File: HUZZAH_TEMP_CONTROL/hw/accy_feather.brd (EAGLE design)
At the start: 50.8 x 22.9 mm, 26 parts

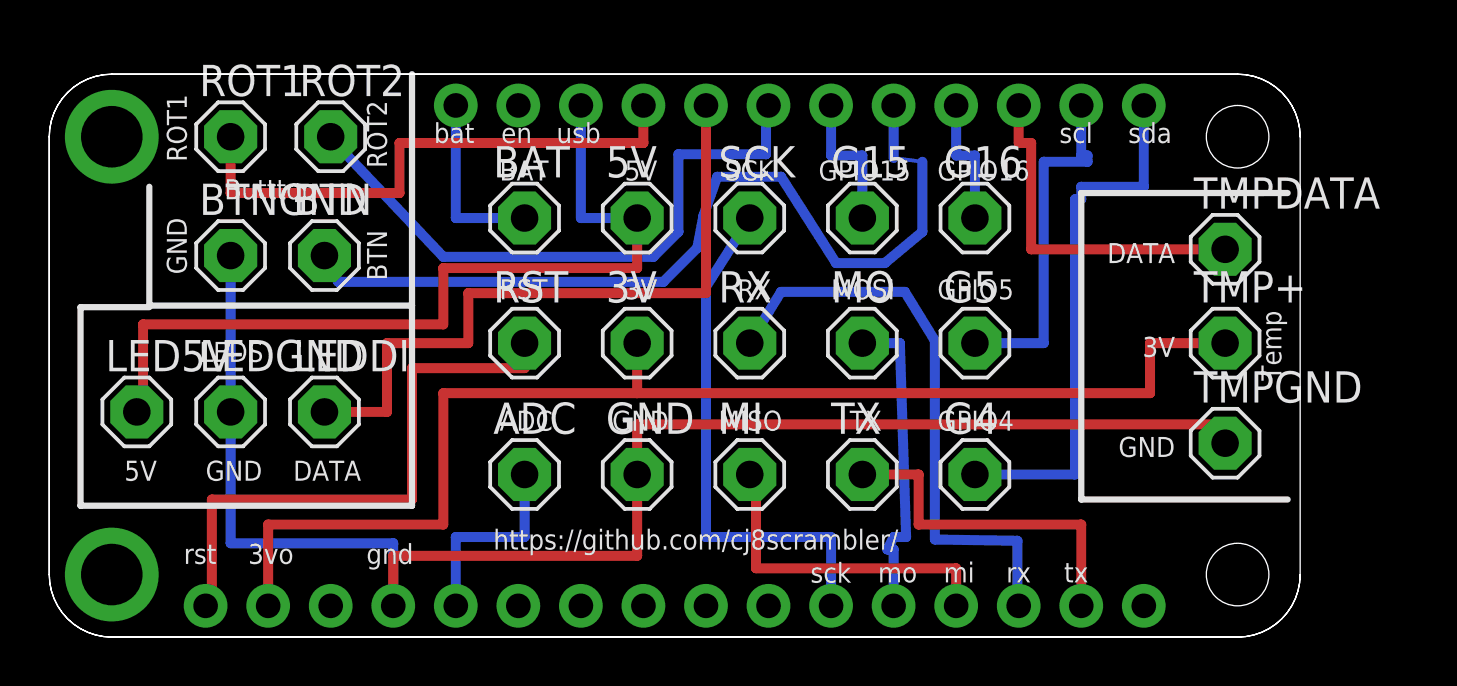
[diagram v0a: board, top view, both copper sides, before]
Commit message: Update feather accy board to v1.1
Added 4.7k pullup on temp data line
Added level shifter on LED data line 3.3v->5V
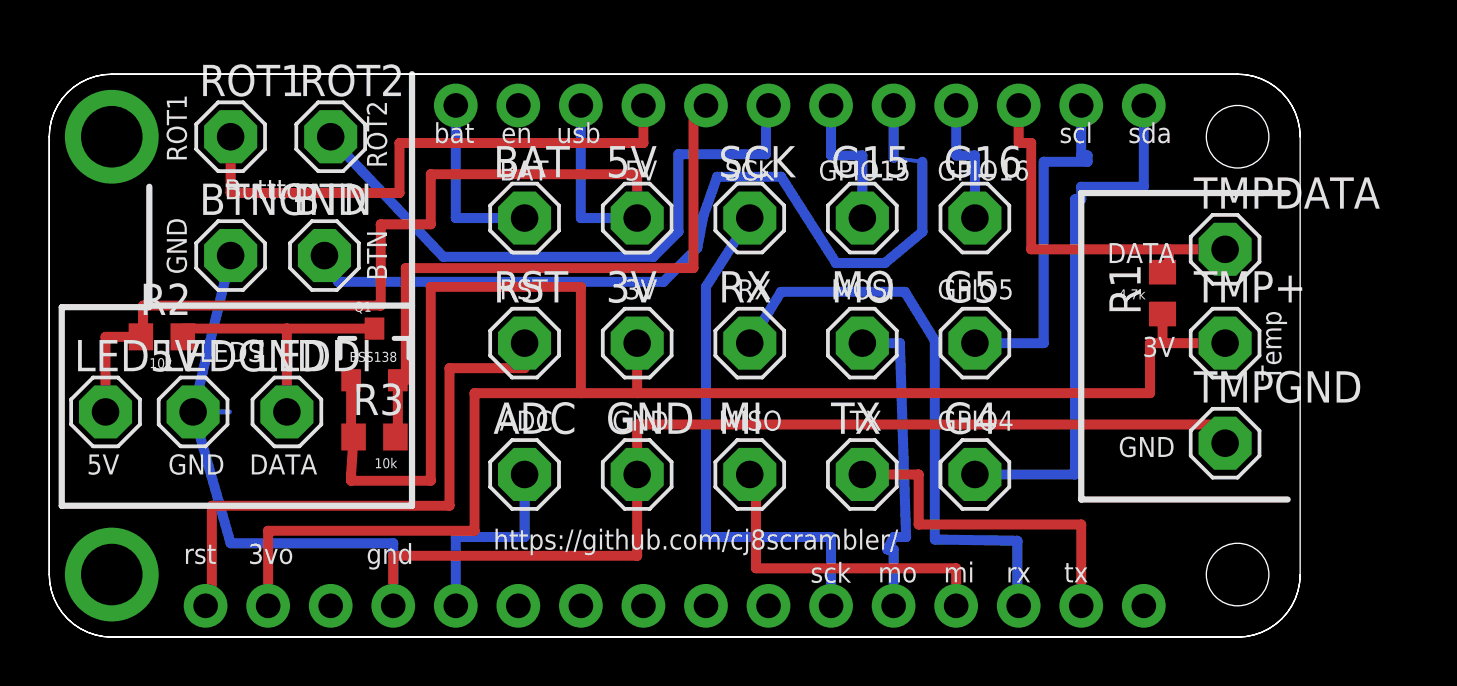
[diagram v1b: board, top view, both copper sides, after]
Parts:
- added Q1: MOSFET-NCHANNELBSS123LT1G, SparkFun-DiscreteSemi:SOT23-3
- added R1: 4.7K, resistor:R0603
- added R2, R3: 10k, resistor:R0603
- moved LEDDI 1.52 mm to (9.65, 9.14)
- moved LEDGND 1.52 mm to (5.84, 9.14)
- moved LED5V 1.27 mm to (2.29, 9.14)
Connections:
- removed net +3V3: 3V.MP, MS1.2, TMP+.MP
- new net N$18: LEDDI.MP, Q1.3, R2.2
- new net N$19: MS1.24, Q1.2, R3.2
- net +5V: now also R2.1
- net N$1: now also R1.2
- net N$6: now also 3V.MP, MS1.2, Q1.1, R1.1, R3.1, TMP+.MP; no longer LEDDI.MP, MS1.24
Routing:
- net +3V3: track 51.6 -> 0.00 mm
- net N$6: track 27.9 -> 78.5 mm
- net N$19: track 0.00 -> 26.1 mm
- net N$18: track 0.00 -> 11.5 mm
- net +5V: track 35.1 -> 39.9 mm
- net GND: track 62.9 -> 64.7 mm
- net N$1: track 14.2 -> 15.4 mm
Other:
- board text added: "10k"
- board text added: "2016 v 1.1"
- board text added: "4.7k"
- board text added: "BSS138"
- board text removed: "2016 v 1.0"

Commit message: Accessory board version 1.2
Removed the MOSFET based level shifter for LED data and replaced
it with a TI TXS01012.  The MOSFET level shifter worked, but it
wasn't fast enough to keep good data integrity for the WS2811 LED
driver.

I also routed the relay control through the same TXS01012 level
shifter so it can be safely used to drive an external SSR instead
of a feather relay board.
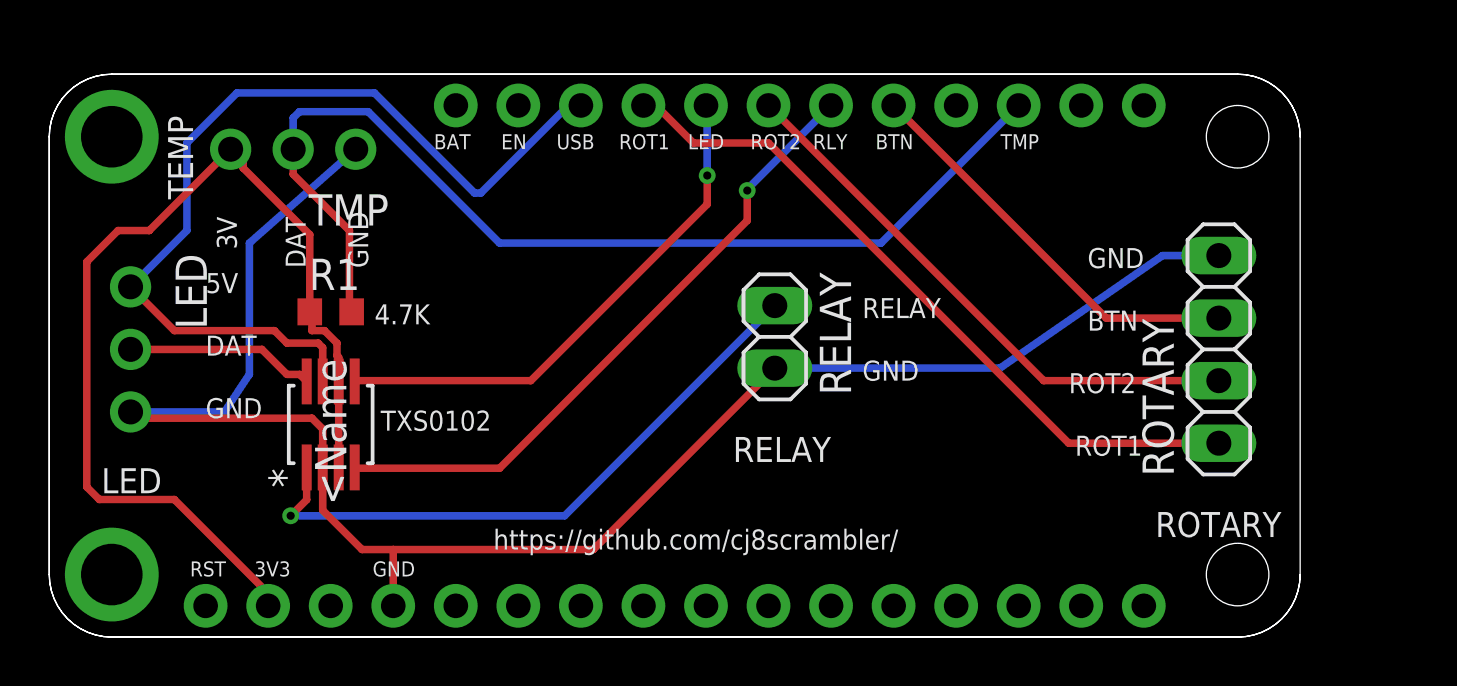
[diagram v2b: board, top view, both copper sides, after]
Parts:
- removed 3V, 5V, ADC, BAT, BTN, BTNGND, G15, G16, G4, G5, GND, LED5V, LEDDI, LEDGND, MI, MO, ROT1, ROT2, RST, RX, SCK, TMP+, TMPDATA, TMPGND, TX: SE11, solpad:SE11
- removed Q1: MOSFET-NCHANNELBSS123LT1G, SparkFun-DiscreteSemi:SOT23-3
- removed R2, R3: 10k, resistor:R0603
- added LED, TMP: (no value), adafruit:1X03-CLEANBIG
- added RELAY: (no value), pinhead:1X02
- added ROTARY: (no value), pinhead:1X04
- added TXS0102: TXS0102DCTRDCT8-M, DZ:DCT8-M
- moved R1 33.8 mm to (11.4, 13.2), turned to 0 degrees
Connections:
- removed net N$1: MS1.19, R1.2, TMPDATA.MP
- removed net N$10: MS1.11, SCK.MP
- removed net N$11: ADC.MP, MS1.5
- removed net N$12: MO.MP, MS1.12
- removed net N$13: MI.MP, MS1.13
- removed net N$14: MS1.14, RX.MP
- removed net N$15: MS1.15, TX.MP
- removed net N$18: LEDDI.MP, Q1.3, R2.2
- removed net N$19: MS1.24, Q1.2, R3.2
- removed net N$2: BTN.MP, MS1.21
- removed net N$3: MS1.23, ROT2.MP
- removed net N$4: G4.MP, MS1.17
- removed net N$5: G5.MP, MS1.18
- removed net N$6: 3V.MP, MS1.2, Q1.1, R1.1, R3.1, TMP+.MP
- removed net N$7: G16.MP, MS1.20
- removed net N$8: G15.MP, MS1.22
- removed net N$9: MS1.1, RST.MP
- removed net VBAT: BAT.MP, MS1.28
- new net +3V3: MS1.2, R1.1, TMP.3, TXS0102.3, TXS0102.6
- new net BTN: MS1.21, ROTARY.3
- new net GPIO12: MS1.24, TXS0102.5
- new net GPIO15: MS1.22, TXS0102.4
- new net LED_DATA: LED.2, TXS0102.8
- new net RELAY: RELAY.1, TXS0102.1
- new net ROT1: MS1.25, ROTARY.1
- new net TMP_DATA: MS1.19, R1.2, TMP.2
- net +5V: now also LED.1, TXS0102.7; no longer 5V.MP, LED5V.MP, R2.1
- net GND: now also LED.3, RELAY.2, ROTARY.4, TMP.1, TXS0102.2; no longer BTNGND.MP, GND.MP, LEDGND.MP, TMPGND.MP
- net ROT2: now also MS1.23, ROTARY.2; no longer MS1.25, ROT1.MP
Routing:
- net N$6: track 78.5 -> 0.00 mm
- net TMP_DATA: track 0.00 -> 43.0 mm
- net +3V3: track 0.00 -> 41.6 mm
- net N$2: track 36.2 -> 0.00 mm
- net ROT1: track 0.00 -> 29.0 mm
- net GPIO15: track 0.00 -> 26.3 mm, vias 0 -> 1
- net N$19: track 26.1 -> 0.00 mm
- net RELAY: track 0.00 -> 25.4 mm, vias 0 -> 1
- net N$3: track 25.4 -> 0.00 mm
- net N$14: track 23.9 -> 0.00 mm
- net N$9: track 23.6 -> 0.00 mm
- net N$4: track 21.8 -> 0.00 mm
- net GPIO12: track 0.00 -> 21.5 mm, vias 0 -> 1
- net N$10: track 21.3 -> 0.00 mm
- net BTN: track 0.00 -> 16.8 mm
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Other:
- board text added: "2017 v 1.2"
- board text added: "4.7K"
- board text added: "DAT"
- board text added: "EN"
- board text added: "LED"
- board text added: "Networked temp controller accessory feather"
- board text added: "RELAY"
- board text added: "RLY"
- board text added: "ROTARY"
- board text added: "TEMP"
- board text added: "TMP"
- board text added: "TXS0102"
- board text added: "USB"
- board text removed: "10k"
- board text removed: "2016 v 1.1"
- board text removed: "3vo"
- board text removed: "4.7k"
- board text removed: "ADC"
- board text removed: "BSS138"
- board text removed: "BUTTON"
- board text removed: "Buttton"
- board text removed: "DATA"
- board text removed: "G15"
- board text removed: "G16"
- board text removed: "G4"
- board text removed: "G5"
- board text removed: "GPIO15"
- board text removed: "GPIO16"
- board text removed: "GPIO4"
- board text removed: "GPIO5"
- board text removed: "Huzzah Temp Control Feather Accessory Wing"
- board text removed: "LEDS"
- board text removed: "MISO"
- board text removed: "MOSI"
- board text removed: "RX"
- board text removed: "SCK"
- board text removed: "TX"
- board text removed: "Temp"
- board text removed: "bat"
- board text removed: "en"
- board text removed: "gnd"
- board text removed: "mi"
- board text removed: "mo"
- board text removed: "rst"
- board text removed: "rx"
- board text removed: "sck"
- board text removed: "scl"
- board text removed: "sda"
- board text removed: "tx"
- board text removed: "usb"

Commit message: Accessory board version 2.0
Added a pulldown on the high voltage side of the relay output.  This
is needed because the level shifter can drive it high when it's floating
which causes board instability.

Added on-board 10A relay (Digi-Key Part #Z2763-ND) to the bottom side.
There are 2 choices for relay control now:
  - You can place the "Relay Drive" header and wire an external relay
    or SSR.  This is a good choice for high current loads like compressors.
                                   or
  - You can place the 10 relay Digi-Key Part #Z2763-ND) and the
    "Relay Switch" header.  The externally switched power can be run
    through the "Relay Switch" header.  This is good for lower current
    resistive heaters.
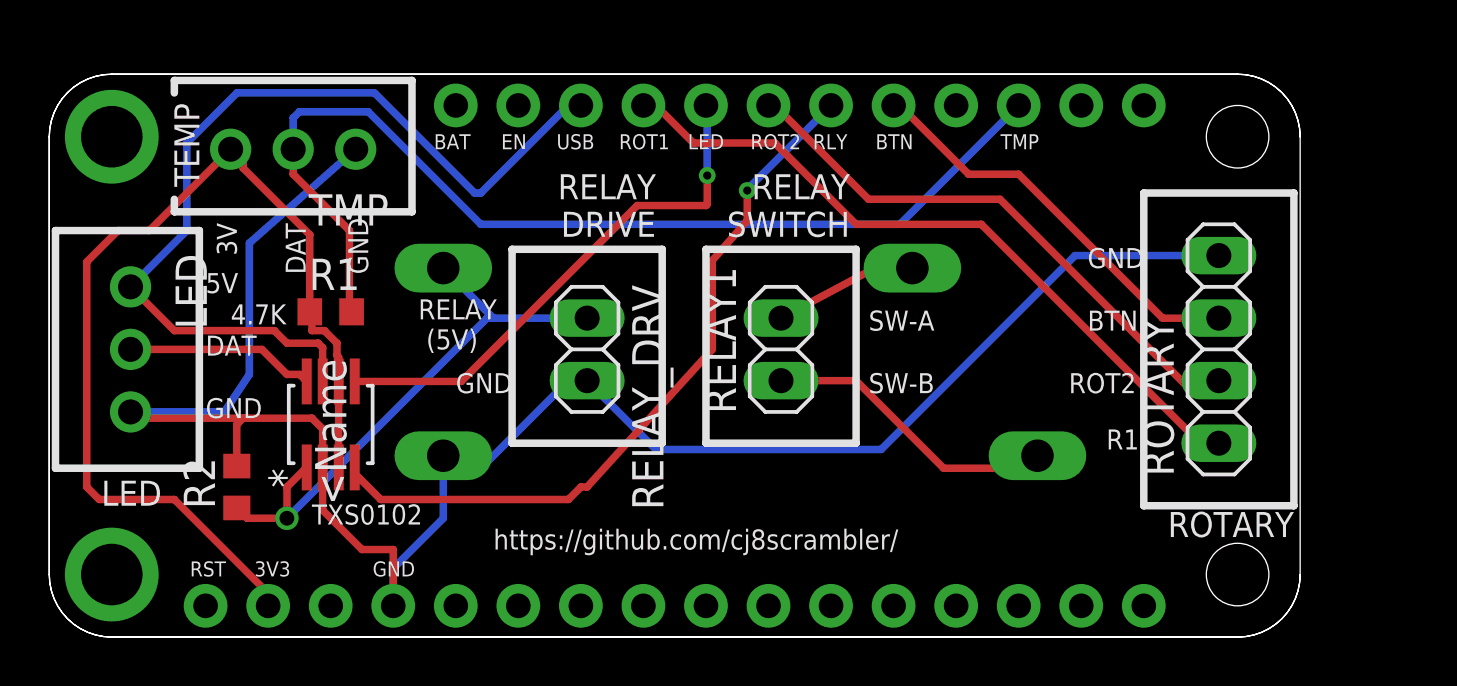
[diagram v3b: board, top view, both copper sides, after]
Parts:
- removed RELAY: (no value), pinhead:1X02
- added K1: G6RS, relay:G6RS
- added R2: 10k, resistor:R0603
- added RELAY1: RELAY_OUT, pinhead:1X02
- added RELAY_DRV: RELAY_DRIVE, pinhead:1X02
- LED: value (none) -> LED
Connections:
- new net N$2: K1.P, RELAY1.2
- new net RELAY_CTRL: K1.S, RELAY1.1
- net GND: now also K1.2, R2.2, RELAY_DRV.2; no longer RELAY.2
- net RELAY: now also K1.1, R2.1, RELAY_DRV.1; no longer RELAY.1
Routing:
- net RELAY_CTRL: track 0.00 -> 12.1 mm
- net GND: track 71.9 -> 80.5 mm
- net N$2: track 0.00 -> 5.84 mm
- net GPIO15: track 26.3 -> 29.9 mm
- net RELAY: track 25.4 -> 23.0 mm
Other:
- board text added: "2017 v 2.0"
- board text added: "R1"
- board text added: "R2"
- board text added: "RELAY (5V)"
- board text added: "RELAY DRIVE"
- board text added: "RELAY SWITCH"
- board text added: "RELAY_DRV"
- board text added: "SW-A"
- board text added: "SW-B"
- board text removed: "2017 v 1.2"
- board text removed: "RELAY"

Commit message: Accessory board version 2.1
Moved relay to a transistor based 1-way level shifter.  The
2-way level shifter was causing problems with boot mode pins.
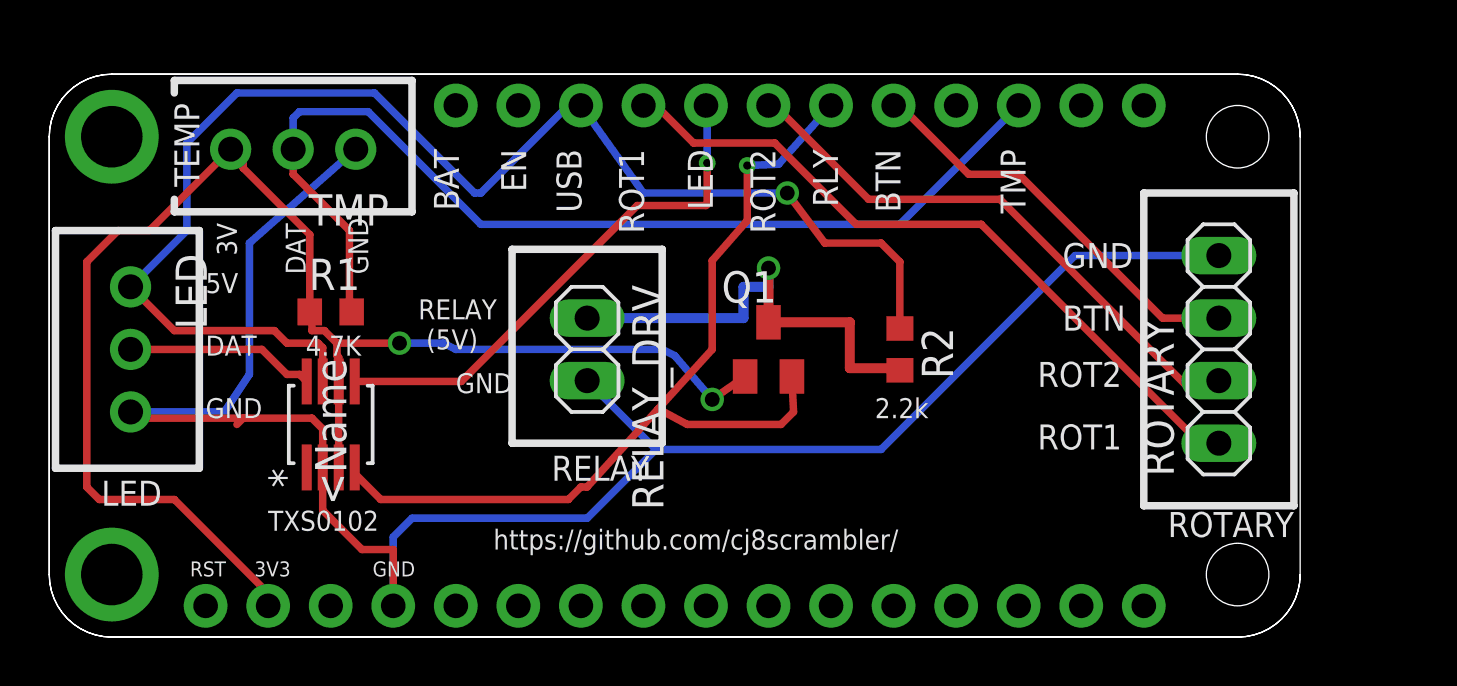
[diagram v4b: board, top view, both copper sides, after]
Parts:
- removed K1: G6RS, relay:G6RS
- removed RELAY1: RELAY_OUT, pinhead:1X02
- added Q1: BSS123, transistor-small-signal:SOT23
- R2: value 10k -> 2.2k
- moved R2 27.5 mm to (34.5, 11.7), turned to 270 degrees
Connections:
- removed net N$2: K1.P, RELAY1.2
- removed net RELAY: K1.1, R2.1, RELAY_DRV.1, TXS0102.1
- removed net RELAY_CTRL: K1.S, RELAY1.1
- new net N$1: Q1.3, R2.2, RELAY_DRV.1
- net +3V3: now also Q1.1
- net +5V: now also R2.1
- net GND: no longer K1.2, R2.2
- net GPIO15: now also Q1.2; no longer TXS0102.4
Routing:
- net RELAY: track 23.0 -> 0.00 mm, vias 1 -> 0
- net N$1: track 0.00 -> 18.9 mm, vias 0 -> 1
- net +5V: track 37.0 -> 55.8 mm, vias 0 -> 1
- net +3V3: track 41.6 -> 59.4 mm, vias 0 -> 2
- net RELAY_CTRL: track 12.1 -> 0.00 mm
- net GPIO15: track 29.9 -> 37.5 mm
- net N$2: track 5.84 -> 0.00 mm
- net GND: track 80.5 -> 79.3 mm
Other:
- board text added: "2.2k"
- board text added: "2017 v 2.1"
- board text added: "RELAY"
- board text removed: "2017 v 2.0"
- board text removed: "RELAY DRIVE"
- board text removed: "RELAY SWITCH"
- board text removed: "SW-A"
- board text removed: "SW-B"
